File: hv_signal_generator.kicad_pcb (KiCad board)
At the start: 2 copper layers, 83.8 x 56.1 mm, 57 parts, among them IC1 ATMEG328PU, J2 COMM_BUS, P1 FTDI_USB, P2 ISP, P3 POWER, P4 VOUT, P5 LIGHT, P6 MAGNET, Q1 IRF644PBF, Q2 P16NF06, SW1 RESET, U1 HV513, U2 MAX1771, U3 MCP41050, U4 HV7802, U5 AQW216, X1 16MHz

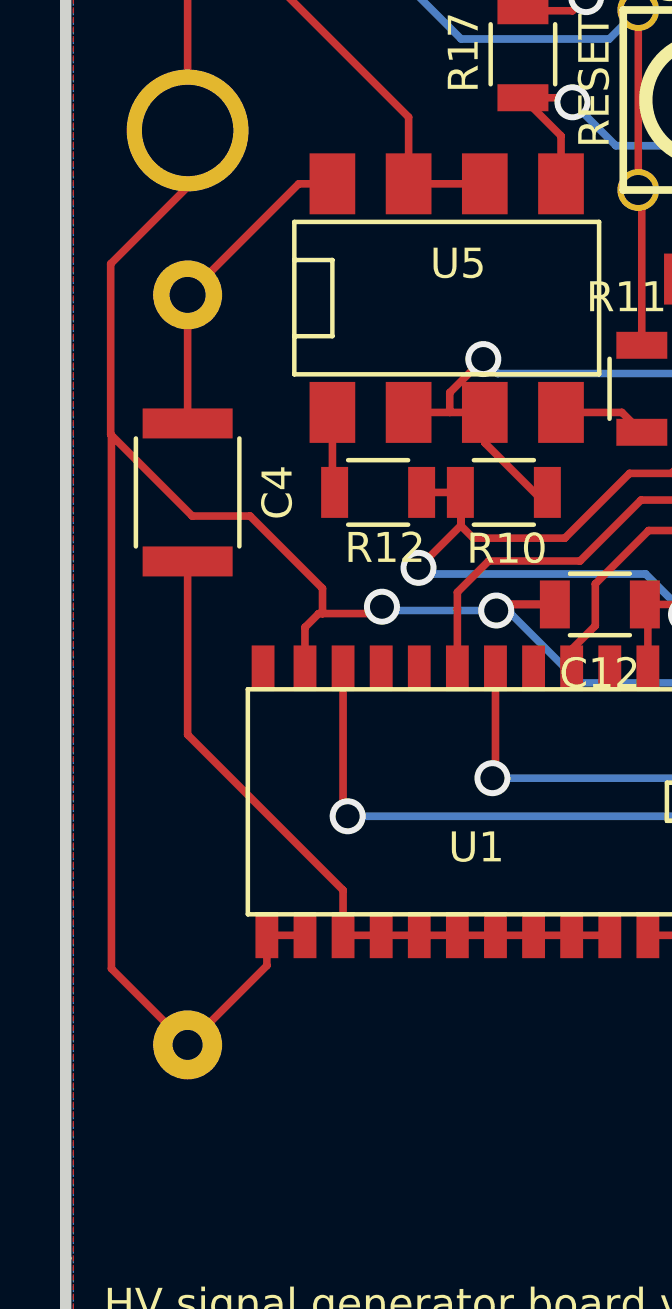
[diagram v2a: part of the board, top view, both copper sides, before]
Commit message: Add clearance between VOUT pin and screw
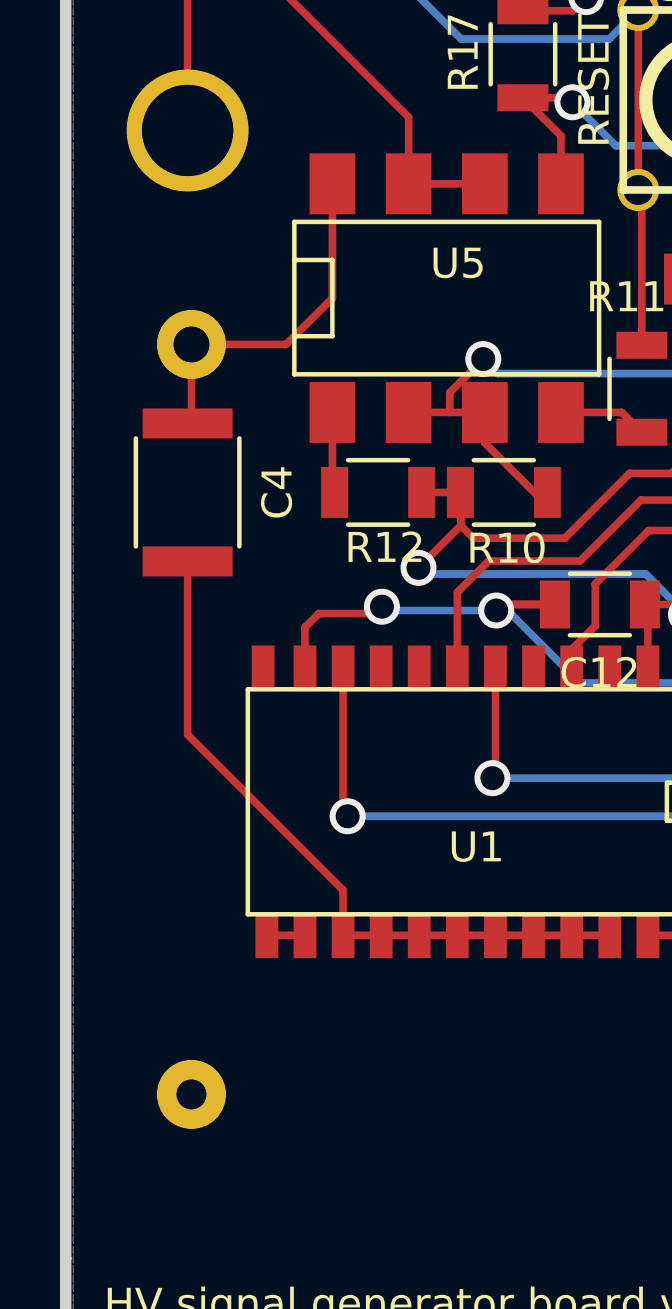
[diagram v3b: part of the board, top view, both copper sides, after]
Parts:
- moved R18 1.66 mm to (20.4, 62.6)
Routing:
- net GND: track 287.7 -> 242.2 mm
- net VOUT: track 10.6 -> 11.8 mm
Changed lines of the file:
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@@
     (thickness 1.6002)
     (drawings 9)
-    (tracks 618)
+    (tracks 609)
     (zones 0)
     (modules 57)
@@
     (mod_text_size 1.524 1.524)
     (mod_text_width 0.3048)
-    (pad_size 2.3 1.3)
-    (pad_drill 0.8)
+    (pad_size 6 6)
+    (pad_drill 3.048)
     (pad_to_mask_clearance 0.254)
     (aux_axis_origin 0 0)
@@
     (add_net VOUT)
   )
+  (module Resistors_ThroughHole:Resistor_Horizontal_RM25mm (layer Back)
+    (at 20.447 62.611 90)
+    (descr "Resistor, Axial, RM 25mm,")
+    (tags "Resistor Axial RM 25mm")
+    (fp_text reference R18 (at 12.49934 5.75056 90) (layer B.SilkS)
+      (effects (font (size 1 1) (thickness 0.15)) (justify mirror))
+    )
+    (fp_text value 10k (at 12.7 -2.032 90) (layer B.Fab)
+      (effects (font (size 1 1) (thickness 0.15)) (justify mirror))
+    )
+    (fp_line (start -1.4 4.05) (end 26.4 4.05) (layer B.CrtYd) (width 0.05))
+    (fp_line (start -1.4 -4.05) (end -1.4 4.05) (layer B.CrtYd) (width 0.05))
+    (fp_line (start 26.4 4.05) (end 26.4 -4.05) (layer B.CrtYd) (width 0.05))
+    (fp_line (start -1.4 -4.05) (end 26.4 -4.05) (layer B.CrtYd) (width 0.05))
+    (fp_line (start 3.556 0) (end 1.524 0) (layer B.SilkS) (width 0.15))
+    (fp_line (start 21.844 0) (end 23.368 0) (layer B.SilkS) (width 0.15))
+    (fp_line (start 3.81 3.81) (end 3.81 -3.81) (layer B.SilkS) (width 0.15))
+    (fp_line (start 3.81 -3.81) (end 21.59 -3.81) (layer B.SilkS) (width 0.15))
+    (fp_line (start 21.59 -3.81) (end 21.59 3.81) (layer B.SilkS) (width 0.15))
+    (fp_line (start 21.59 3.81) (end 3.81 3.81) (layer B.SilkS) (width 0.15))
+    (pad 1 thru_hole circle (at 0 0 90) (size 2.30124 2.30124) (drill 1.00076) (layers *.Cu *.SilkS *.Mask)
+      (net 1 GND))
+    (pad 2 thru_hole circle (at 24.99868 0 90) (size 2.30124 2.30124) (drill 1.19888) (layers *.Cu *.SilkS *.Mask)
+      (net 53 VOUT))
+  )
   (module Capacitors_SMD:C_1812 (layer Front)
     (at 55.88 56.388 180)
@@
       (rotate (xyz 0 0 0))
     )
-  )
-  (module Resistors_ThroughHole:Resistor_Horizontal_RM25mm (layer Back)
-    (at 20.32 60.96 90)
-    (descr "Resistor, Axial, RM 25mm,")
-    (tags "Resistor Axial RM 25mm")
-    (fp_text reference R18 (at 12.49934 5.75056 90) (layer B.SilkS)
-      (effects (font (size 1 1) (thickness 0.15)) (justify mirror))
-    )
-    (fp_text value 10k (at 12.7 -2.032 90) (layer B.Fab)
-      (effects (font (size 1 1) (thickness 0.15)) (justify mirror))
-    )
-    (fp_line (start -1.4 4.05) (end 26.4 4.05) (layer B.CrtYd) (width 0.05))
-    (fp_line (start -1.4 -4.05) (end -1.4 4.05) (layer B.CrtYd) (width 0.05))
-    (fp_line (start 26.4 4.05) (end 26.4 -4.05) (layer B.CrtYd) (width 0.05))
-    (fp_line (start -1.4 -4.05) (end 26.4 -4.05) (layer B.CrtYd) (width 0.05))
-    (fp_line (start 3.556 0) (end 1.524 0) (layer B.SilkS) (width 0.15))
-    (fp_line (start 21.844 0) (end 23.368 0) (layer B.SilkS) (width 0.15))
-    (fp_line (start 3.81 3.81) (end 3.81 -3.81) (layer B.SilkS) (width 0.15))
-    (fp_line (start 3.81 -3.81) (end 21.59 -3.81) (layer B.SilkS) (width 0.15))
-    (fp_line (start 21.59 -3.81) (end 21.59 3.81) (layer B.SilkS) (width 0.15))
-    (fp_line (start 21.59 3.81) (end 3.81 3.81) (layer B.SilkS) (width 0.15))
-    (pad 1 thru_hole circle (at 0 0 90) (size 2.30124 2.30124) (drill 1.00076) (layers *.Cu *.SilkS *.Mask)
-      (net 1 GND))
-    (pad 2 thru_hole circle (at 24.99868 0 90) (size 2.30124 2.30124) (drill 1.19888) (layers *.Cu *.SilkS *.Mask)
-      (net 53 VOUT))
   )
   (module Capacitors_SMD:C_1206 (layer Front)
@@
   (via (at 47.244 66.294) (size 1.2) (drill 0.8) (layers Front Back) (net 1))
   (segment (start 47.0684 66.1184) (end 47.244 66.294) (width 0.254) (layer Front) (net 1))
-  (segment (start 17.78 40.64) (end 17.78 58.42) (width 0.254) (layer Front) (net 1))
-  (segment (start 17.78 58.42) (end 20.32 60.96) (width 0.254) (layer Front) (net 1))
   (segment (start 86.614 19.304) (end 88.392 19.304) (width 0.254) (layer Back) (net 1))
   (segment (start 96.52 27.432) (end 96.52 30.48) (width 0.254) (layer Back) (net 1))
@@
   (segment (start 61.595 20.955) (end 61.595 20.9042) (width 0.254) (layer Back) (net 1))
   (segment (start 20.32 30.48) (end 20.32 32.3596) (width 0.254) (layer Front) (net 1))
-  (segment (start 20.32 32.3596) (end 17.7546 34.925) (width 0.254) (layer Front) (net 1))
-  (segment (start 24.8158 45.7454) (end 24.8158 46.5836) (width 0.254) (layer Front) (net 1))
-  (segment (start 22.4028 43.3324) (end 24.8158 45.7454) (width 0.254) (layer Front) (net 1))
-  (segment (start 20.4724 43.3324) (end 22.4028 43.3324) (width 0.254) (layer Front) (net 1))
-  (segment (start 17.7546 40.6146) (end 17.78 40.64) (width 0.254) (layer Front) (net 1))
-  (segment (start 17.78 40.64) (end 20.4724 43.3324) (width 0.254) (layer Front) (net 1))
-  (segment (start 17.7546 34.925) (end 17.7546 40.6146) (width 0.254) (layer Front) (net 1))
   (segment (start 24.2316 48.4074) (end 24.2316 47.0408) (width 0.254) (layer Front) (net 1))
   (segment (start 24.6888 46.5836) (end 24.8158 46.5836) (width 0.254) (layer Front) (net 1))
   (segment (start 24.2316 47.0408) (end 24.6888 46.5836) (width 0.254) (layer Front) (net 1))
-  (segment (start 22.9616 57.3074) (end 22.9616 58.3184) (width 0.254) (layer Front) (net 1))
-  (segment (start 22.9616 58.3184) (end 20.32 60.96) (width 0.254) (layer Front) (net 1))
   (segment (start 22.9616 57.3074) (end 24.2316 57.3074) (width 0.254) (layer Front) (net 1))
   (segment (start 61.595 36.83) (end 61.595 36.9316) (width 0.254) (layer Back) (net 1) (status 30))
@@
   (segment (start 92.71 37.87902) (end 92.71 39.825) (width 0.254) (layer Front) (net 51) (status 30))
   (segment (start 97.155 37.87902) (end 97.155 39.825) (width 0.254) (layer Front) (net 52) (status 30))
-  (segment (start 20.32 35.96132) (end 20.32 40.245) (width 0.254) (layer Front) (net 53) (status 30))
-  (segment (start 25.146 32.258) (end 24.02332 32.258) (width 0.254) (layer Front) (net 53) (status 10))
-  (segment (start 24.02332 32.258) (end 20.32 35.96132) (width 0.254) (layer Front) (net 53) (status 20))
+  (segment (start 20.447 37.61232) (end 20.447 40.118) (width 0.254) (layer Front) (net 53))
+  (segment (start 20.447 40.118) (end 20.32 40.245) (width 0.254) (layer Front) (net 53))
+  (segment (start 20.447 37.61232) (end 23.60168 37.61232) (width 0.254) (layer Front) (net 53))
+  (segment (start 25.146 36.068) (end 25.146 32.258) (width 0.254) (layer Front) (net 53))
+  (segment (start 23.60168 37.61232) (end 25.146 36.068) (width 0.254) (layer Front) (net 53))
   (segment (start 74.094 47.752) (end 74.094 53.012) (width 0.254) (layer Front) (net 54))
   (segment (start 74.803 53.721) (end 75.852 53.721) (width 0.254) (layer Front) (net 54))

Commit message: [WIP] Remove HV513, fix orientation of FTDI header
* fix footprint of L1
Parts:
- removed 1PIN (x2): P***, 1pin
- removed C12: 0.1uF, Capacitors_SMD:C_1206
- removed C4: 0.1uF, Capacitors_SMD:C_1812
- removed R18: 10k, Resistors_ThroughHole:Resistor_Horizontal_RM25mm
- removed U1: HV513, footprints:SOW-24
- C7: value 4u7,250V -> 10uF,250V; footprint Capacitors_SMD:c_elec_8x10.5 -> Capacitors_SMD:c_elec_10x10
- L1: footprint Inductors:self_cms_we-pd3 -> footprints:DU1971
- R11, R12: value 375 -> 374
- R13: value 5k -> 5.1k
- R14: value 5 -> 5.1
- R15, R17: value 50k -> 51k
- R9: value 40k -> 39k
- moved C3 12.0 mm to (43.4, 25.2), turned to 180 degrees
- moved JP1 9.54 mm to (34.5, 22.4), turned to 90 degrees
- moved L1 4.07 mm to (86.5, 64.5)
- moved C6 1.94 mm to (91.8, 53.6)
- moved C7 1.52 mm to (55.2, 65.0)
- moved C1 0.99 mm to (84.7, 52.8)
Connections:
- P1 pad 1: Net-(C3-Pad1) -> GND
- P1 pad 2: RX -> Net-(P1-Pad2)
- P1 pad 3: TX -> +5V_USB
- P1 pad 4: +5V_USB -> TX
- P1 pad 5: Net-(P1-Pad5) -> RX
- P1 pad 6: GND -> Net-(C3-Pad1)
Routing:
- net D7/HV513_CS: track 58.3 -> 0.00 mm, vias 2 -> 0
- net D9/S_MOSI: track 85.3 -> 29.4 mm, vias 3 -> 2
- net D6/BL: track 50.3 -> 0.00 mm, vias 2 -> 0
- net D8/S_SCK: track 65.8 -> 21.1 mm, vias 3 -> 2
- net GND: track 242.2 -> 206.2 mm, vias 22 -> 19
- net Net-(C4-Pad2): track 24.7 -> 0.00 mm
- net Net-(C7-Pad1): track 66.7 -> 51.4 mm
- net +5V: track 231.2 -> 217.7 mm, vias 6 -> 5
- net VOUT: track 11.8 -> 0.00 mm
- net Net-(D1-Pad2): track 23.9 -> 12.2 mm
- net HV: track 10.9 -> 3.12 mm
- net RST: track 72.8 -> 65.9 mm
- net RX: track 25.7 -> 22.0 mm
- net TX: track 25.2 -> 21.9 mm, vias 1 -> 0
- net Net-(C3-Pad1): track 2.42 -> 5.40 mm
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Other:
- net class Default: clearance 0.4 -> 0.127
- rule trace_clearance: 0.4 -> 0.127

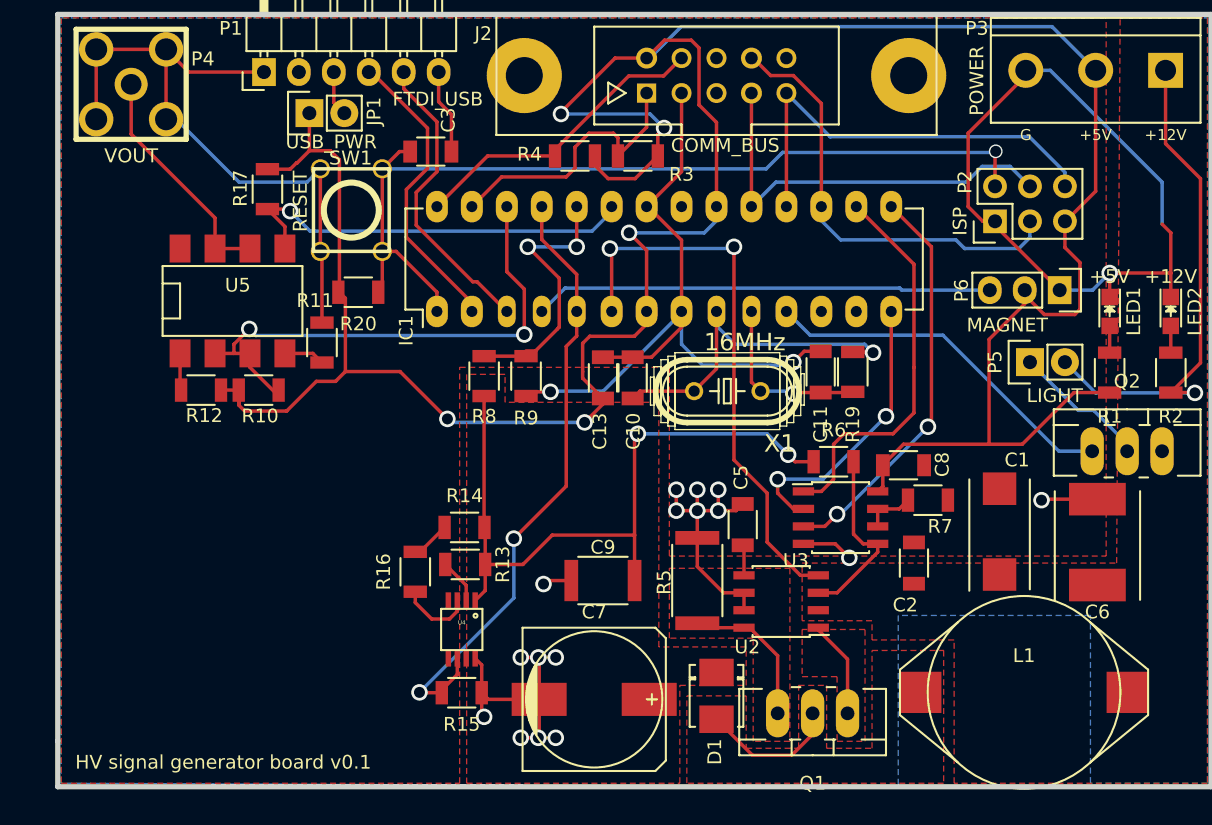
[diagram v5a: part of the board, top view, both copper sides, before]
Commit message: [WIP] Add hv signal generator breakout headers
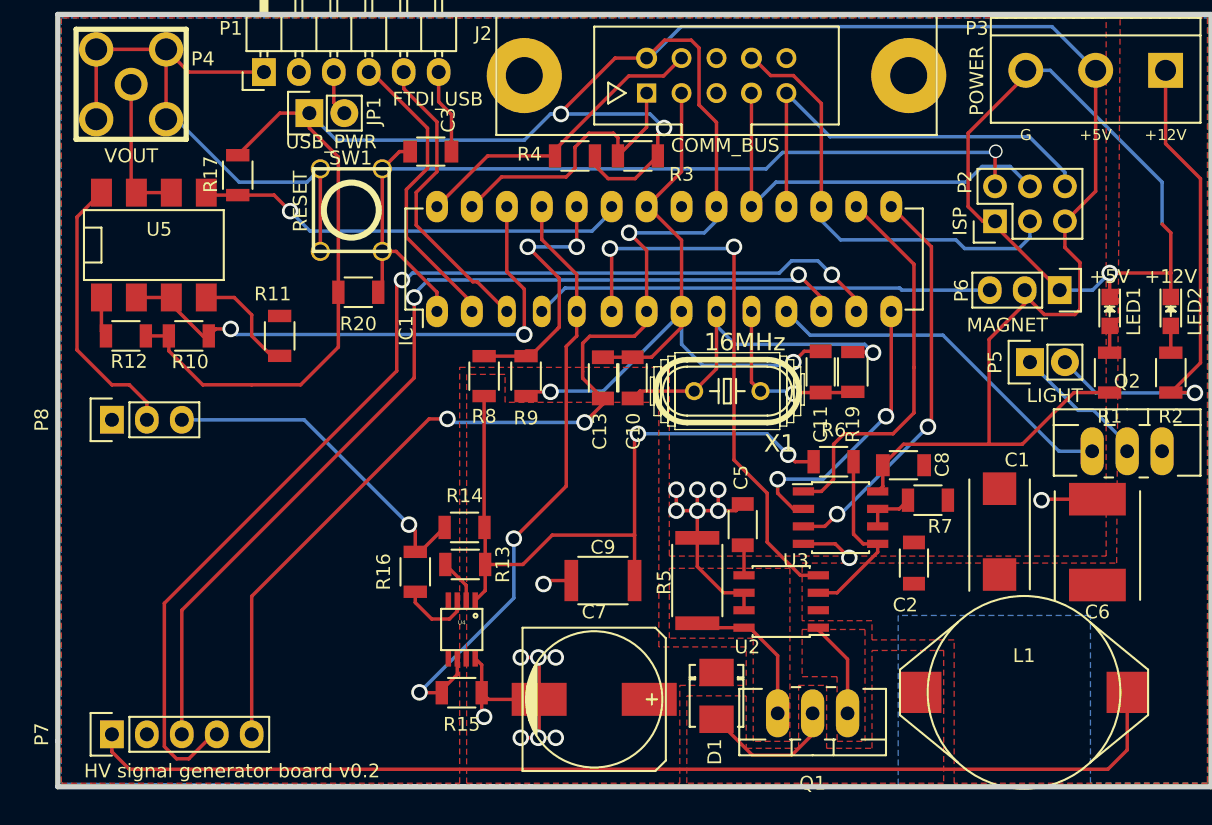
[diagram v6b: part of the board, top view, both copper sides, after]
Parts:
- added P7: CONN_01X05, Pin_Headers:Pin_Header_Straight_1x05, F.Cu at (20.2, 67.6)
- added P8: CONN_01X03, Pin_Headers:Pin_Header_Straight_1x03, F.Cu at (20.2, 44.7)
- moved U5 7.01 mm to (23.2, 32.0)
- moved R12 6.73 mm to (21.2, 38.6)
- moved R10 6.43 mm to (25.8, 38.6)
- moved R11 3.11 mm to (32.4, 38.6)
- moved R17 2.39 mm to (29.3, 26.9)
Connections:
- IC1 pad 12: D6/BL -> D6
- IC1 pad 13: D7/HV513_CS -> D7
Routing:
- net D7: track 0.00 -> 81.6 mm, vias 0 -> 2
- net +12V: track 37.5 -> 117.9 mm
- net D6: track 0.00 -> 70.9 mm, vias 0 -> 2
- net +5V: track 217.7 -> 263.4 mm
- net HV: track 3.12 -> 25.0 mm, vias 0 -> 1
- net VOUT: track 0.00 -> 20.1 mm
- net Net-(P4-Pad1): track 17.0 -> 10.6 mm
- net GND: track 206.2 -> 201.1 mm
- net Net-(R11-Pad2): track 2.97 -> 7.98 mm
- net A0/SHORT_CHK: track 30.0 -> 31.6 mm
- net A3/OUTPUT_SELECT: track 38.9 -> 40.0 mm
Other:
- board text added: "HV signal generator board v0.2"
- board text removed: "HV signal generator board v0.1"

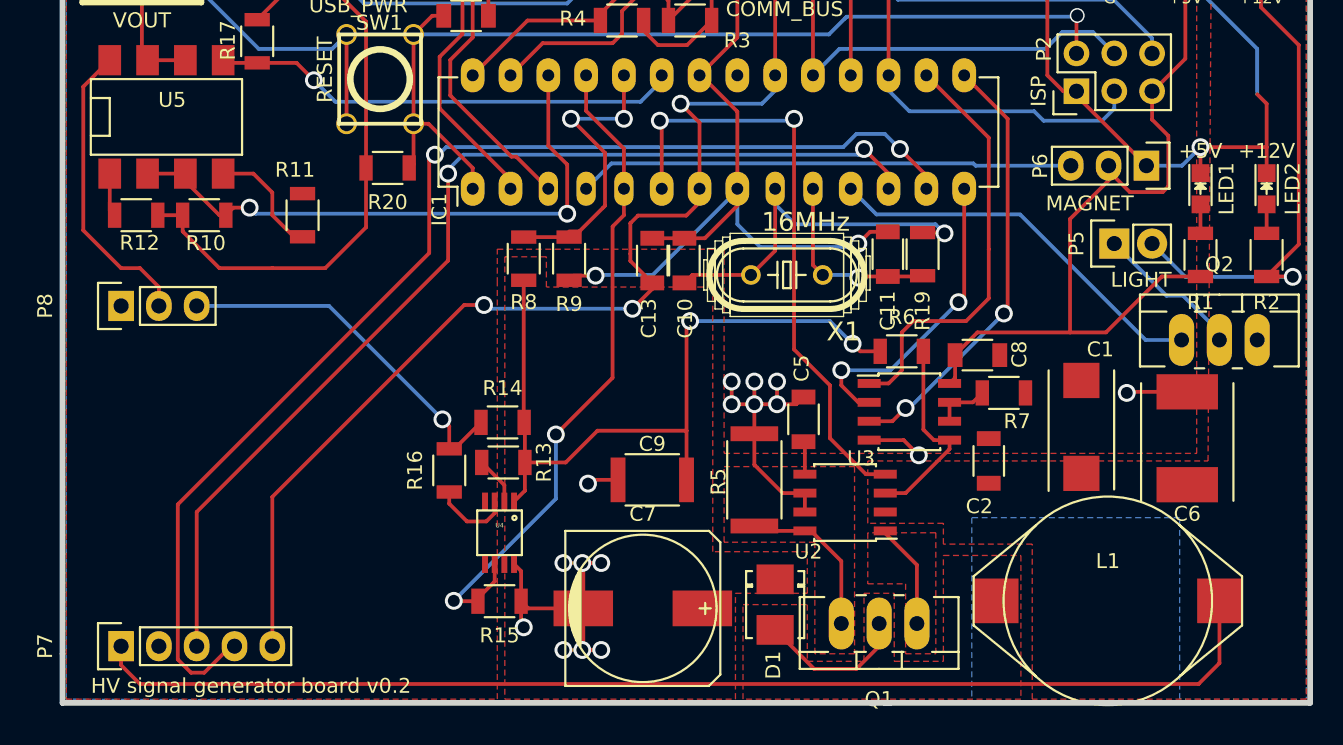
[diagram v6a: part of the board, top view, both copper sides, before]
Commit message: Swap parts to support up to 400V and use BJT for LED
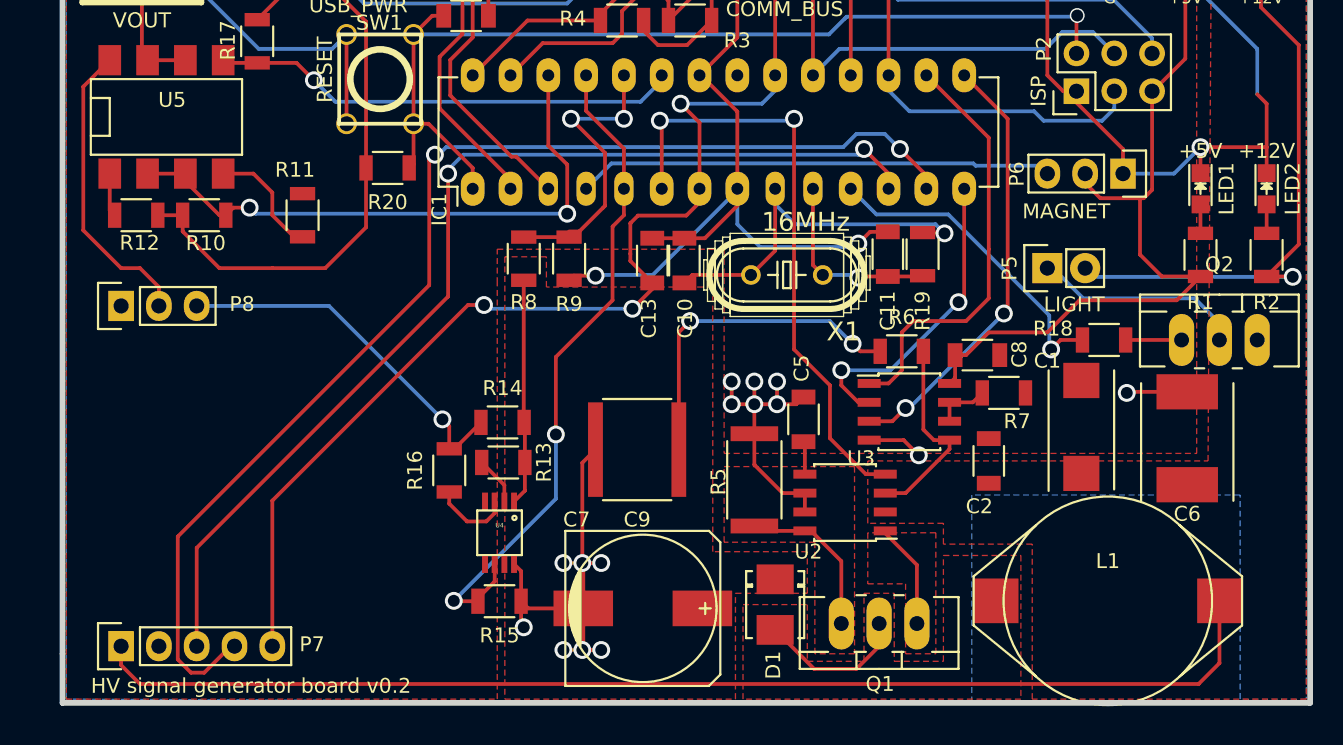
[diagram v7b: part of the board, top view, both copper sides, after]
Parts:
- added R18: 1k, Resistors_SMD:R_1206, F.Cu at (86.2, 47.0)
- C7: value 10uF,250V -> 3.3uF,400V
- C9: value 100nF,250V -> 100nF,400V; footprint Capacitors_SMD:C_1812 -> Capacitors_SMD:C_2225
- Q2: value P16NF06 -> TIP120
- R6, R8: value 2M -> 1M
- R7: value 10k -> 4k
- R9: value 39k -> 20k
- moved P5 4.79 mm to (82.4, 42.2)
- moved C9 2.27 mm to (54.9, 54.4)
- moved P6 1.66 mm to (87.5, 35.8)
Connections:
- Q2 pad 1: D5/LED -> Net-(Q2-Pad1)
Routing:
- net Net-(C7-Pad1): track 51.4 -> 37.8 mm
- net GND: track 201.1 -> 207.6 mm, vias 19 -> 18
- net D5/LED: track 26.4 -> 21.6 mm, vias 0 -> 1
- net Net-(P5-Pad1): track 12.2 -> 16.4 mm
- net +12V: track 117.9 -> 121.7 mm
- net Net-(Q2-Pad1): track 0.00 -> 3.76 mm
- net +5V: track 263.4 -> 260.0 mm
- net D2/SERVO: track 33.3 -> 32.0 mm
